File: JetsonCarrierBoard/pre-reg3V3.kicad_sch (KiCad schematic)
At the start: 19 parts

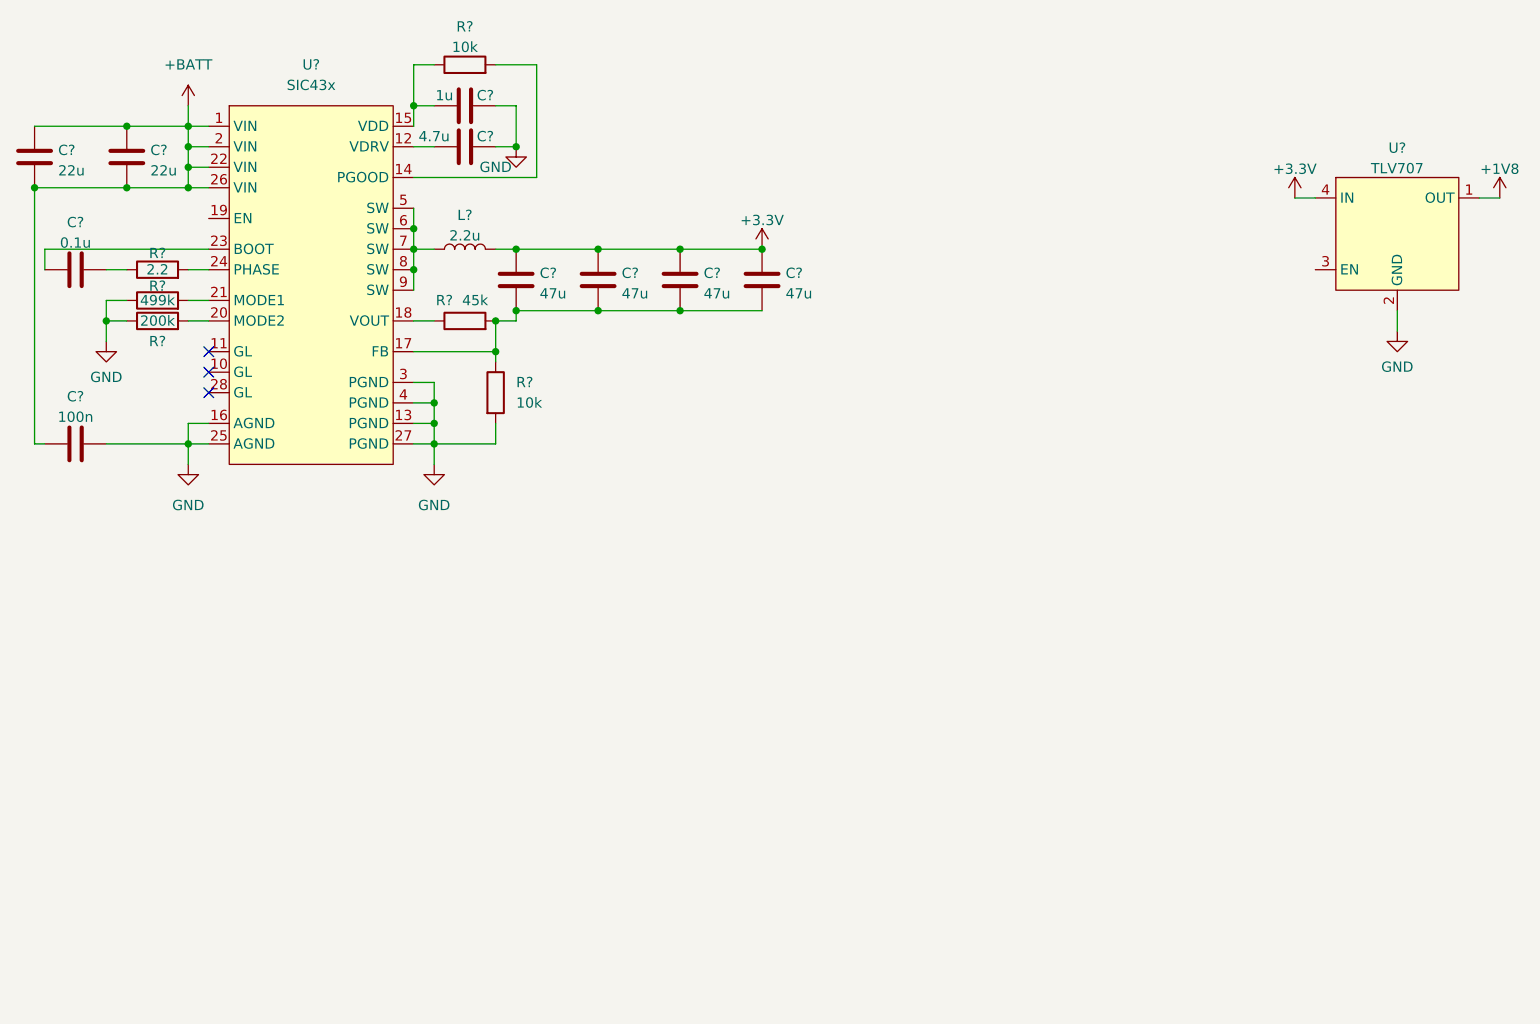
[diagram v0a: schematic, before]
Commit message: Part 2 of USB C wiring, renaming schematics
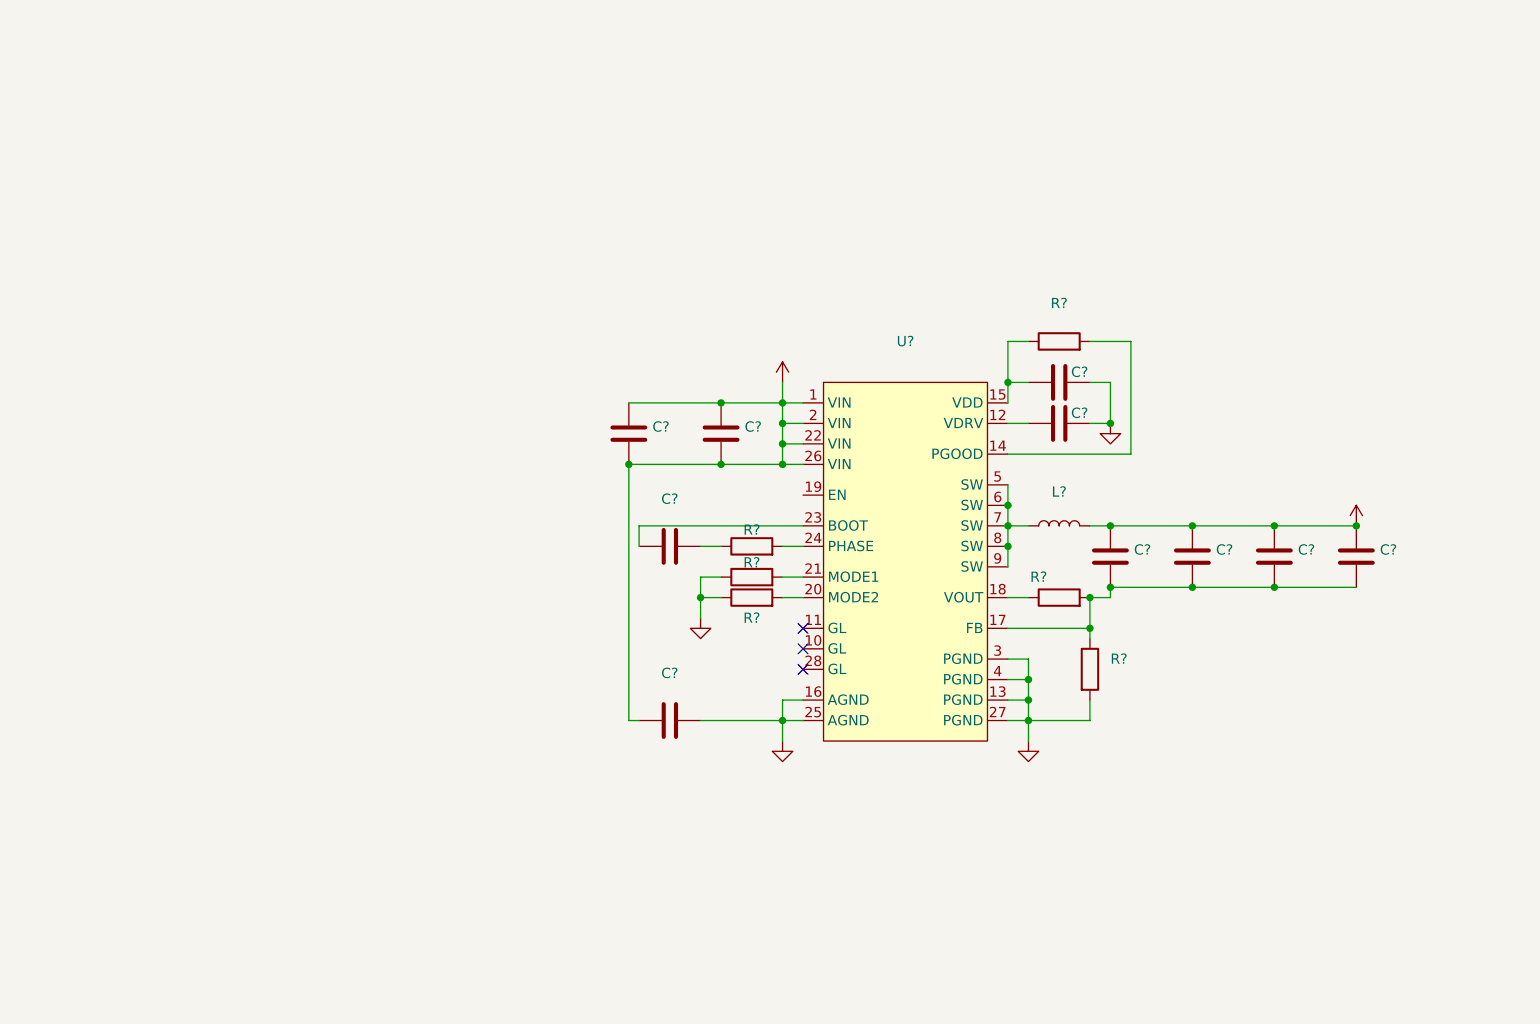
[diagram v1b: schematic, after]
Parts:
- removed U?: TLV707, symbol Voltage_Regulators_Linear:TLV707
- C?: value 100n -> (none)
- C? (x4): value 47u -> (none)
- C?: value 1u -> (none)
- C? (x2): value 22u -> (none)
- C?: value 0.1u -> (none)
- C?: value 4.7u -> (none)
- L?: value 2.2u -> (none)
- R?: value 45k -> (none)
- R?: value 2.2 -> (none)
- R? (x2): value 10k -> (none)
- R?: value 499k -> (none)
- R?: value 200k -> (none)
- U?: value SIC43x -> (none)
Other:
- moved on the sheet: C?, L?, R?, U?

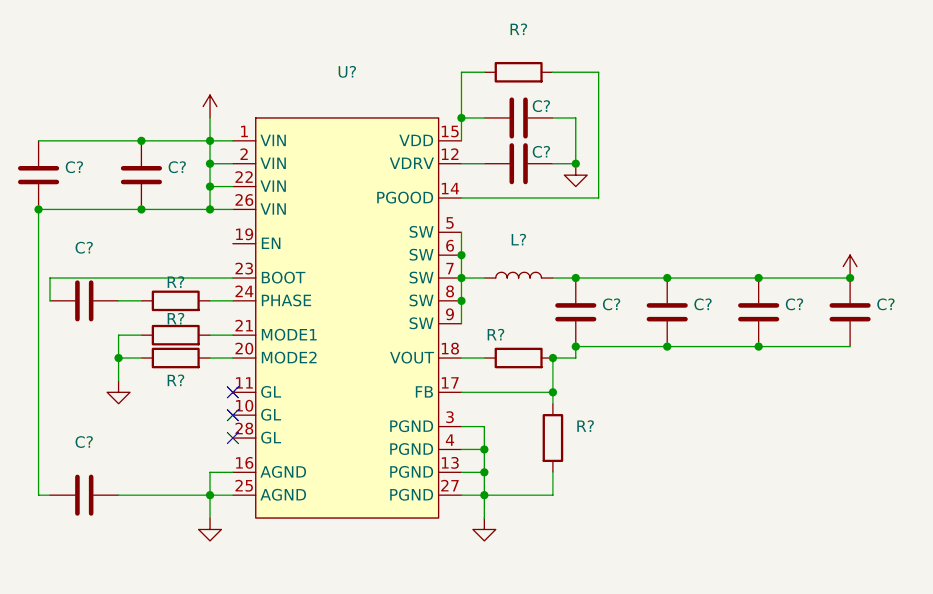
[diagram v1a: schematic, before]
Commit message: Finished USB-C w/ Alt mode and PD Wiring V1
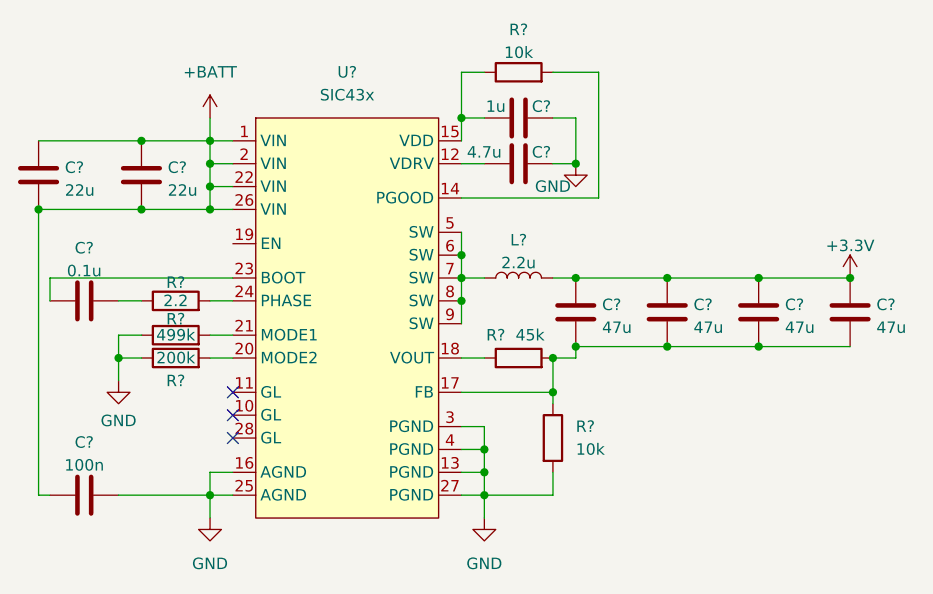
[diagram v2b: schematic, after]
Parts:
- C?: value (none) -> 100n
- C? (x4): value (none) -> 47u
- C?: value (none) -> 1u
- C? (x2): value (none) -> 22u
- C?: value (none) -> 0.1u
- C?: value (none) -> 4.7u
- L?: value (none) -> 2.2u
- R?: value (none) -> 45k
- R?: value (none) -> 2.2
- R? (x2): value (none) -> 10k
- R?: value (none) -> 499k
- R?: value (none) -> 200k
- U?: value (none) -> SIC43x
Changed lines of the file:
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@@
     (in_bom yes) (on_board yes) (fields_autoplaced)
     (property "Reference" "C?" (id 0) (at 115.57 117.3312 90))
-    (property "Value" "" (id 1) (at 115.57 119.8681 90))
+    (property "Value" "100n" (id 1) (at 115.57 119.8681 90))
     (property "Footprint" "" (id 2) (at 119.38 122.2248 0)
       (effects (font (size 1.27 1.27)) hide)
@@
       (effects (font (size 1.27 1.27)) hide)
     )
-    (property "Value" "" (id 1) (at 167.64 88.9 0))
+    (property "Value" "GND" (id 1) (at 167.64 88.9 0))
     (property "Footprint" "" (id 2) (at 170.18 86.36 0)
       (effects (font (size 1.27 1.27)) hide)
@@
       (effects (font (size 1.27 1.27)) hide)
     )
-    (property "Value" "" (id 1) (at 129.54 130.81 0))
+    (property "Value" "GND" (id 1) (at 129.54 130.81 0))
     (property "Footprint" "" (id 2) (at 129.54 125.73 0)
       (effects (font (size 1.27 1.27)) hide)
@@
       (effects (font (size 1.27 1.27)) (justify left))
     )
-    (property "Value" "" (id 1) (at 183.261 104.5722 0)
+    (property "Value" "47u" (id 1) (at 183.261 104.5722 0)
       (effects (font (size 1.27 1.27)) (justify left))
     )
@@
     (in_bom yes) (on_board yes)
     (property "Reference" "R?" (id 0) (at 161.29 105.41 90))
-    (property "Value" "" (id 1) (at 165.1 105.41 90))
+    (property "Value" "45k" (id 1) (at 165.1 105.41 90))
     (property "Footprint" "" (id 2) (at 163.83 109.728 90)
       (effects (font (size 1.27 1.27)) hide)
@@
       (effects (font (size 1.27 1.27)) hide)
     )
-    (property "Value" "" (id 1) (at 200.66 95.4842 0))
+    (property "Value" "+3.3V" (id 1) (at 200.66 95.4842 0))
     (property "Footprint" "" (id 2) (at 200.66 99.06 0)
       (effects (font (size 1.27 1.27)) hide)
@@
     (in_bom yes) (on_board yes) (fields_autoplaced)
     (property "Reference" "L?" (id 0) (at 163.83 94.8522 90))
-    (property "Value" "" (id 1) (at 163.83 97.3891 90))
+    (property "Value" "2.2u" (id 1) (at 163.83 97.3891 90))
     (property "Footprint" "" (id 2) (at 163.83 99.06 0)
       (effects (font (size 1.27 1.27)) hide)
@@
     (in_bom yes) (on_board yes)
     (property "Reference" "R?" (id 0) (at 125.73 99.568 90))
-    (property "Value" "" (id 1) (at 125.73 101.6 90))
+    (property "Value" "2.2" (id 1) (at 125.73 101.6 90))
     (property "Footprint" "" (id 2) (at 125.73 103.378 90)
       (effects (font (size 1.27 1.27)) hide)
@@
     (in_bom yes) (on_board yes) (fields_autoplaced)
     (property "Reference" "R?" (id 0) (at 163.83 71.4842 90))
-    (property "Value" "" (id 1) (at 163.83 74.0211 90))
+    (property "Value" "10k" (id 1) (at 163.83 74.0211 90))
     (property "Footprint" "" (id 2) (at 163.83 77.978 90)
       (effects (font (size 1.27 1.27)) hide)
@@
       (effects (font (size 1.27 1.27)) hide)
     )
-    (property "Value" "" (id 1) (at 160.02 130.81 0))
+    (property "Value" "GND" (id 1) (at 160.02 130.81 0))
     (property "Footprint" "" (id 2) (at 160.02 125.73 0)
       (effects (font (size 1.27 1.27)) hide)
@@
     (in_bom yes) (on_board yes)
     (property "Reference" "R?" (id 0) (at 125.73 103.632 90))
-    (property "Value" "" (id 1) (at 125.73 105.41 90))
+    (property "Value" "499k" (id 1) (at 125.73 105.41 90))
     (property "Footprint" "" (id 2) (at 125.73 107.188 90)
       (effects (font (size 1.27 1.27)) hide)
@@
     (in_bom yes) (on_board yes)
     (property "Reference" "R?" (id 0) (at 125.73 110.49 90))
-    (property "Value" "" (id 1) (at 125.73 107.95 90))
+    (property "Value" "200k" (id 1) (at 125.73 107.95 90))
     (property "Footprint" "" (id 2) (at 125.73 109.728 90)
       (effects (font (size 1.27 1.27)) hide)
@@
     (in_bom yes) (on_board yes)
     (property "Reference" "C?" (id 0) (at 166.37 80.01 90))
-    (property "Value" "" (id 1) (at 161.29 80.01 90))
+    (property "Value" "1u" (id 1) (at 161.29 80.01 90))
     (property "Footprint" "" (id 2) (at 167.64 80.3148 0)
       (effects (font (size 1.27 1.27)) hide)
@@
       (effects (font (size 1.27 1.27)) (justify left))
     )
-    (property "Value" "" (id 1) (at 113.411 89.3322 0)
+    (property "Value" "22u" (id 1) (at 113.411 89.3322 0)
       (effects (font (size 1.27 1.27)) (justify left))
     )
@@
       (effects (font (size 1.27 1.27)) (justify left))
     )
-    (property "Value" "" (id 1) (at 124.841 89.3322 0)
+    (property "Value" "22u" (id 1) (at 124.841 89.3322 0)
       (effects (font (size 1.27 1.27)) (justify left))
     )
@@
       (effects (font (size 1.27 1.27)) hide)
     )
-    (property "Value" "" (id 1) (at 129.54 76.2 0))
+    (property "Value" "+BATT" (id 1) (at 129.54 76.2 0))
     (property "Footprint" "" (id 2) (at 129.54 81.28 0)
       (effects (font (size 1.27 1.27)) hide)
@@
     (in_bom yes) (on_board yes) (fields_autoplaced)
     (property "Reference" "C?" (id 0) (at 115.57 95.7412 90))
-    (property "Value" "" (id 1) (at 115.57 98.2781 90))
+    (property "Value" "0.1u" (id 1) (at 115.57 98.2781 90))
     (property "Footprint" "" (id 2) (at 119.38 100.6348 0)
       (effects (font (size 1.27 1.27)) hide)
@@
     (in_bom yes) (on_board yes) (fields_autoplaced)
     (property "Reference" "U?" (id 0) (at 144.78 76.2 0))
-    (property "Value" "" (id 1) (at 144.78 78.74 0))
+    (property "Value" "SIC43x" (id 1) (at 144.78 78.74 0))
     (property "Footprint" "" (id 2) (at 149.86 82.55 0)
       (effects (font (size 1.27 1.27)) hide)
@@
       (effects (font (size 1.27 1.27)) (justify left))
     )
-    (property "Value" "" (id 1) (at 203.581 104.5722 0)
+    (property "Value" "47u" (id 1) (at 203.581 104.5722 0)
       (effects (font (size 1.27 1.27)) (justify left))
     )
@@
       (effects (font (size 1.27 1.27)) (justify left))
     )
-    (property "Value" "" (id 1) (at 193.421 104.5722 0)
+    (property "Value" "47u" (id 1) (at 193.421 104.5722 0)
       (effects (font (size 1.27 1.27)) (justify left))
     )
@@
       (effects (font (size 1.27 1.27)) (justify left))
     )
-    (property "Value" "" (id 1) (at 170.18 118.1099 0)
+    (property "Value" "10k" (id 1) (at 170.18 118.1099 0)
       (effects (font (size 1.27 1.27)) (justify left))
     )
@@
       (effects (font (size 1.27 1.27)) (justify left))
     )
-    (property "Value" "" (id 1) (at 173.101 104.5722 0)
+    (property "Value" "47u" (id 1) (at 173.101 104.5722 0)
       (effects (font (size 1.27 1.27)) (justify left))
     )
@@
       (effects (font (size 1.27 1.27)) hide)
     )
-    (property "Value" "" (id 1) (at 119.38 114.9334 0))
+    (property "Value" "GND" (id 1) (at 119.38 114.9334 0))
     (property "Footprint" "" (id 2) (at 119.38 110.49 0)
       (effects (font (size 1.27 1.27)) hide)
@@
     (in_bom yes) (on_board yes)
     (property "Reference" "C?" (id 0) (at 166.37 85.09 90))
-    (property "Value" "" (id 1) (at 160.02 85.09 90))
+    (property "Value" "4.7u" (id 1) (at 160.02 85.09 90))
     (property "Footprint" "" (id 2) (at 167.64 85.3948 0)
       (effects (font (size 1.27 1.27)) hide)

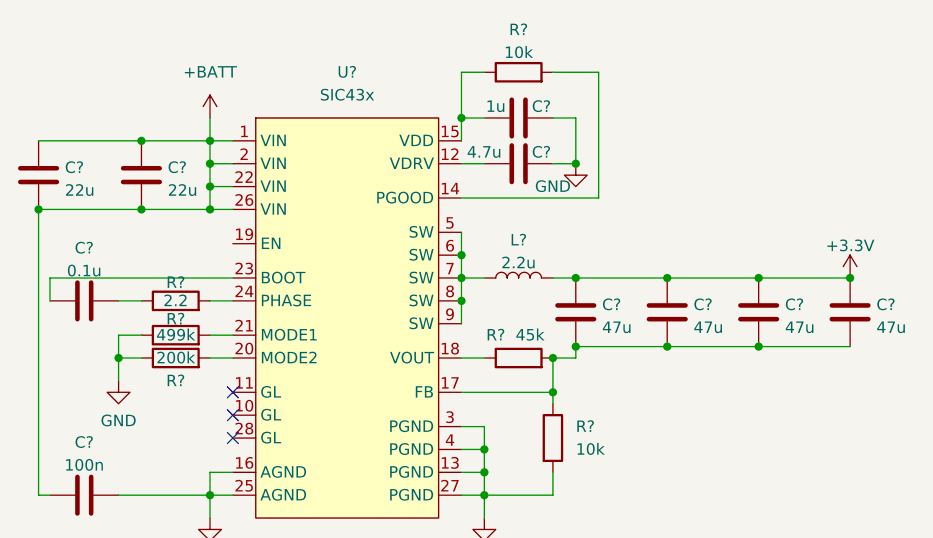
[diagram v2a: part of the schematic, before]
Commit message: Power Sequencing Wiring Part 1
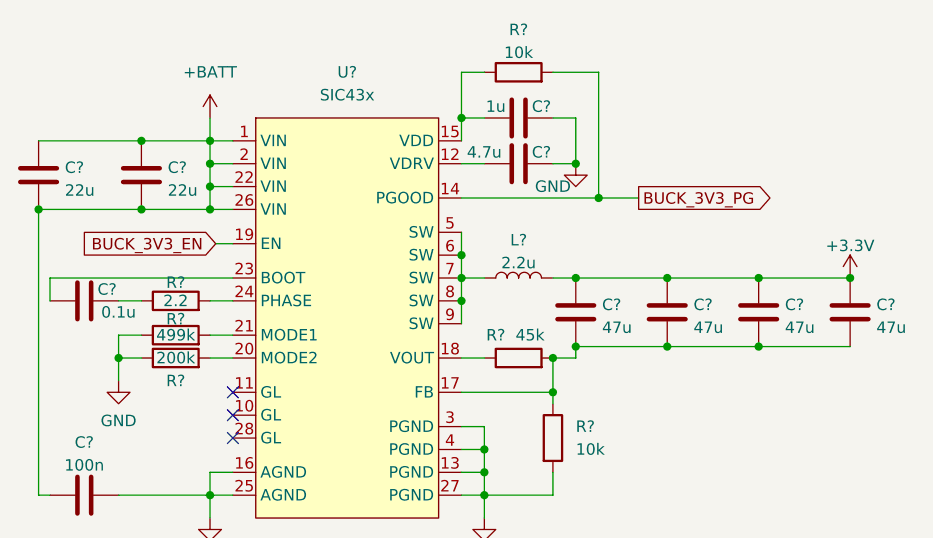
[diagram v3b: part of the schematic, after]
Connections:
- net BUCK_3V3_PG: now reaches R?.2, U?.14 (PGOOD)
- net BUCK_3V3_EN: now reaches U?.19 (EN)
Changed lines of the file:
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@@
   (junction (at 157.48 81.28) (diameter 0) (color 0 0 0 0)
+  )
+  (junction (at 172.72 90.17) (diameter 0) (color 0 0 0 0)
   )
   (junction (at 160.02 123.19) (diameter 0) (color 0 0 0 0)
@@
     (stroke (width 0) (type default) (color 0 0 0 0))
   )
+  (wire (pts (xy 172.72 90.17) (xy 177.165 90.17))
+    (stroke (width 0) (type default) (color 0 0 0 0))
+  )
   (wire (pts (xy 129.54 86.36) (xy 132.08 86.36))
     (stroke (width 0) (type default) (color 0 0 0 0))
@@
     (stroke (width 0) (type default) (color 0 0 0 0))
   )
+  (wire (pts (xy 130.175 95.25) (xy 132.08 95.25))
+    (stroke (width 0) (type default) (color 0 0 0 0))
+  )
   (wire (pts (xy 157.48 93.98) (xy 157.48 96.52))
     (stroke (width 0) (type default) (color 0 0 0 0))
@@
   (wire (pts (xy 129.54 107.95) (xy 132.08 107.95))
     (stroke (width 0) (type default) (color 0 0 0 0))
+  )
+  (global_label "BUCK_3V3_PG" (shape output) (at 177.165 90.17 0) (fields_autoplaced)
+    (effects (font (size 1.27 1.27)) (justify left))
+    (property "Intersheet References" "${INTERSHEET_REFS}" (id 0) (at 192.7014 90.0906 0)
+      (effects (font (size 1.27 1.27)) (justify left) hide)
+    )
+  )
+  (global_label "BUCK_3V3_EN" (shape input) (at 130.175 95.25 180) (fields_autoplaced)
+    (effects (font (size 1.27 1.27)) (justify right))
+    (property "Intersheet References" "${INTERSHEET_REFS}" (id 0) (at 114.699 95.1706 0)
+      (effects (font (size 1.27 1.27)) (justify right) hide)
+    )
   )
   (symbol (lib_id "Device:C") (at 115.57 123.19 90) (unit 1)
@@
   )
   (symbol (lib_id "Device:C") (at 115.57 101.6 90) (unit 1)
-    (in_bom yes) (on_board yes) (fields_autoplaced)
-    (property "Reference" "C?" (id 0) (at 115.57 95.7412 90))
-    (property "Value" "0.1u" (id 1) (at 115.57 98.2781 90))
+    (in_bom yes) (on_board yes)
+    (property "Reference" "C?" (id 0) (at 118.11 100.33 90))
+    (property "Value" "0.1u" (id 1) (at 119.38 102.87 90))
     (property "Footprint" "" (id 2) (at 119.38 100.6348 0)
       (effects (font (size 1.27 1.27)) hide)

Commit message: Adding more Title block info and changing main hierarchical page layout
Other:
- title: (none) -> Pre-Reg 3V3
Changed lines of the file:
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@@
 (kicad_sch (version 20211123) (generator eeschema)
   (paper "A4")
+  (title_block
+    (title "Pre-Reg 3V3")
+    (date "2022-09-18")
+    (rev "1.0")
+  )
   (junction (at 157.48 99.06) (diameter 0) (color 0 0 0 0)
   )
